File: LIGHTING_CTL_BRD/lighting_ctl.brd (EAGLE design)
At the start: 101.6 x 132.1 mm, 146 parts, among them IC1 ATMEGA328PTQFP, IC2 MCP23008, IC3 PCA9865TSSOP28, IC4 MCP2518, IC5 MCP2562FD, IC6 LMR50410, X1 RJ11-4RJ11-4, X10 KEYSTONE_7788, X11 KEYSTONE_7788, X12 KEYSTONE_7788, X13 KEYSTONE_7788, X14 KEYSTONE_7788, X15 KEYSTONE_7788, X16 KEYSTONE_7788, X17 KEYSTONE_7788, X18 KEYSTONE_7788, X19 KEYSTONE_7788, X2 RJ11-4RJ11-4, X20 KEYSTONE_7788, X21 KEYSTONE_7788, X22 KEYSTONE_7788, X23 KEYSTONE_7788, X24 KEYSTONE_7788, X25 KEYSTONE_7788, X26 KEYSTONE_7788, X27 KEYSTONE_7788, X28 KEYSTONE_7788, X29 KEYSTONE_7788, X30 KEYSTONE_7788, X35 KEYSTONE_7788, X36 KEYSTONE_7788, X37 KEYSTONE_7788, X38 KEYSTONE_7788, X43 KEYSTONE_7788, X44 KEYSTONE_7788, X45 KEYSTONE_7788, X46 KEYSTONE_7788, X7 KEYSTONE_7788, X8 KEYSTONE_7788, X9 KEYSTONE_7788

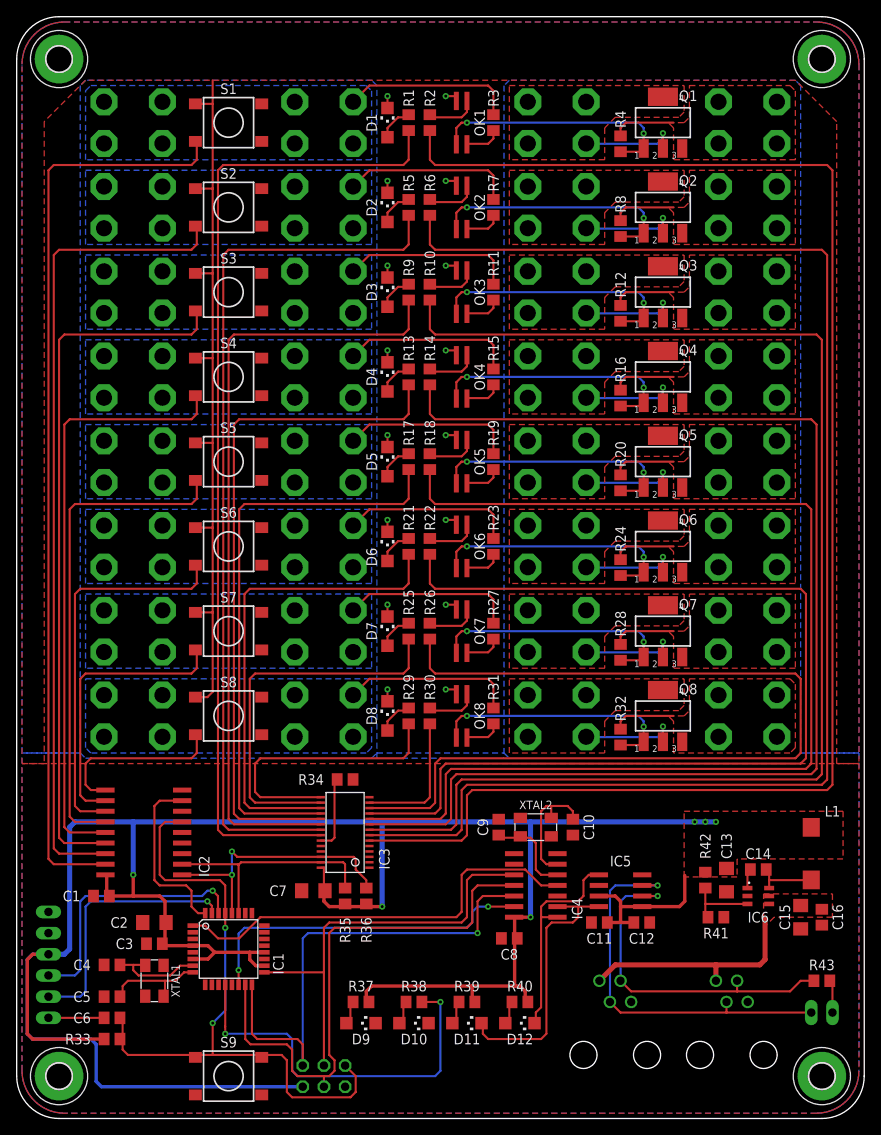
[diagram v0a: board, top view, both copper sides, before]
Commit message: Layout updates for MOSFET & LIGHTING boards. Add new boards REMOTE_SWITCH, CAPACITIVE_SWITCH, VANBUS_HUB
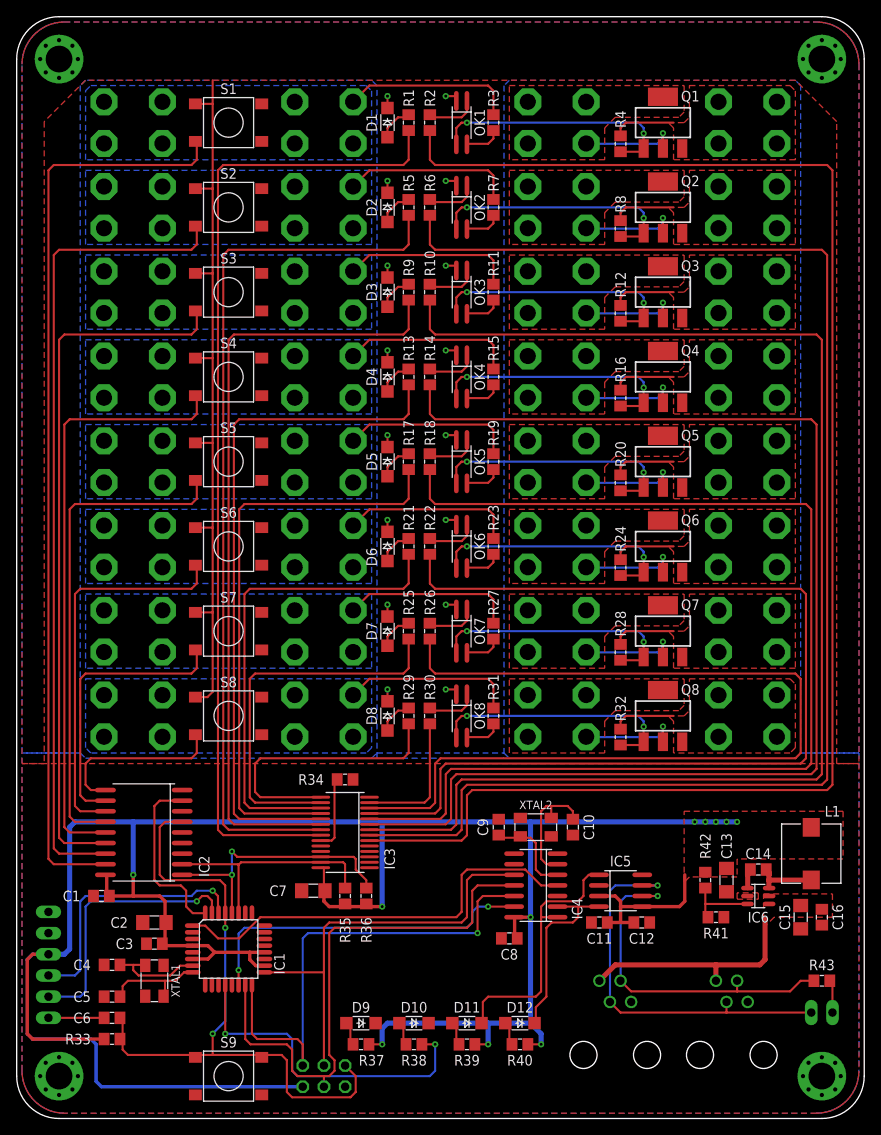
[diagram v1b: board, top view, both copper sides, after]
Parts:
- H1, H2, H3, H4: value MOUNT-PAD-ROUND3.0 -> MOUNT-PAD-ROUND3.2; device holes:3,0-PAD -> THT:3,2-PAD
- OK1, OK2, OK3, OK4, OK5, OK6, OK7, OK8: value (none) -> OPTOCOUPLERSO4
- S1, S2, S3, S4, S5, S6, S7, S8, S9: value (none) -> TACTILE_SWITCH6.2MM
- X1, X2: value RJ11-4RJ11-4 -> RJ11-4HORIZ; device THT:RJ11-4 -> THT:RJ11-4_HORIZ
- moved R37 5.08 mm to (41.3, 8.89)
- moved R38 5.08 mm to (47.6, 8.89)
- moved R39 5.08 mm to (54.0, 8.89)
- moved R40 5.08 mm to (60.3, 8.89)
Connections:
- net GND: now also H1.B3,2, H1.P$1, H1.P$2, H1.P$3, H1.P$4, H1.P$5, H1.P$6, H1.P$7, H1.P$8, H2.B3,2, H2.P$1, H2.P$2, H2.P$3, H2.P$4, H2.P$5, H2.P$6, H2.P$7, H2.P$8, H3.B3,2, H3.P$1, H3.P$2, H3.P$3, H3.P$4, H3.P$5, H3.P$6, H3.P$7, H3.P$8, H4.B3,2, H4.P$1, H4.P$2, H4.P$3, H4.P$4, H4.P$5, H4.P$6, H4.P$7, H4.P$8; no longer H1.B3,0, H2.B3,0, H3.B3,0, H4.B3,0
- net N$18: now also D11.C; no longer D12.C
- net N$19: now also D12.C; no longer D11.C
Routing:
- net VCC: track 297.5 -> 312.9 mm, vias 6 -> 11
- net N$19: track 32.7 -> 22.6 mm
- net LED: track 46.7 -> 40.4 mm
- net N$18: track 25.9 -> 31.9 mm
- net UART_TX: track 31.4 -> 32.3 mm

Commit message: v0.1 Production Run Commit - Including GERBER Files
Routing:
- net INT_CAN: track 51.2 -> 51.4 mm, vias 0 -> 2
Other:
- board text added: "LIGHTING_DIMMER_CONTROLLER_V0.1"
